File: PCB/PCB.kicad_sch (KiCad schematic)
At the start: 0 parts

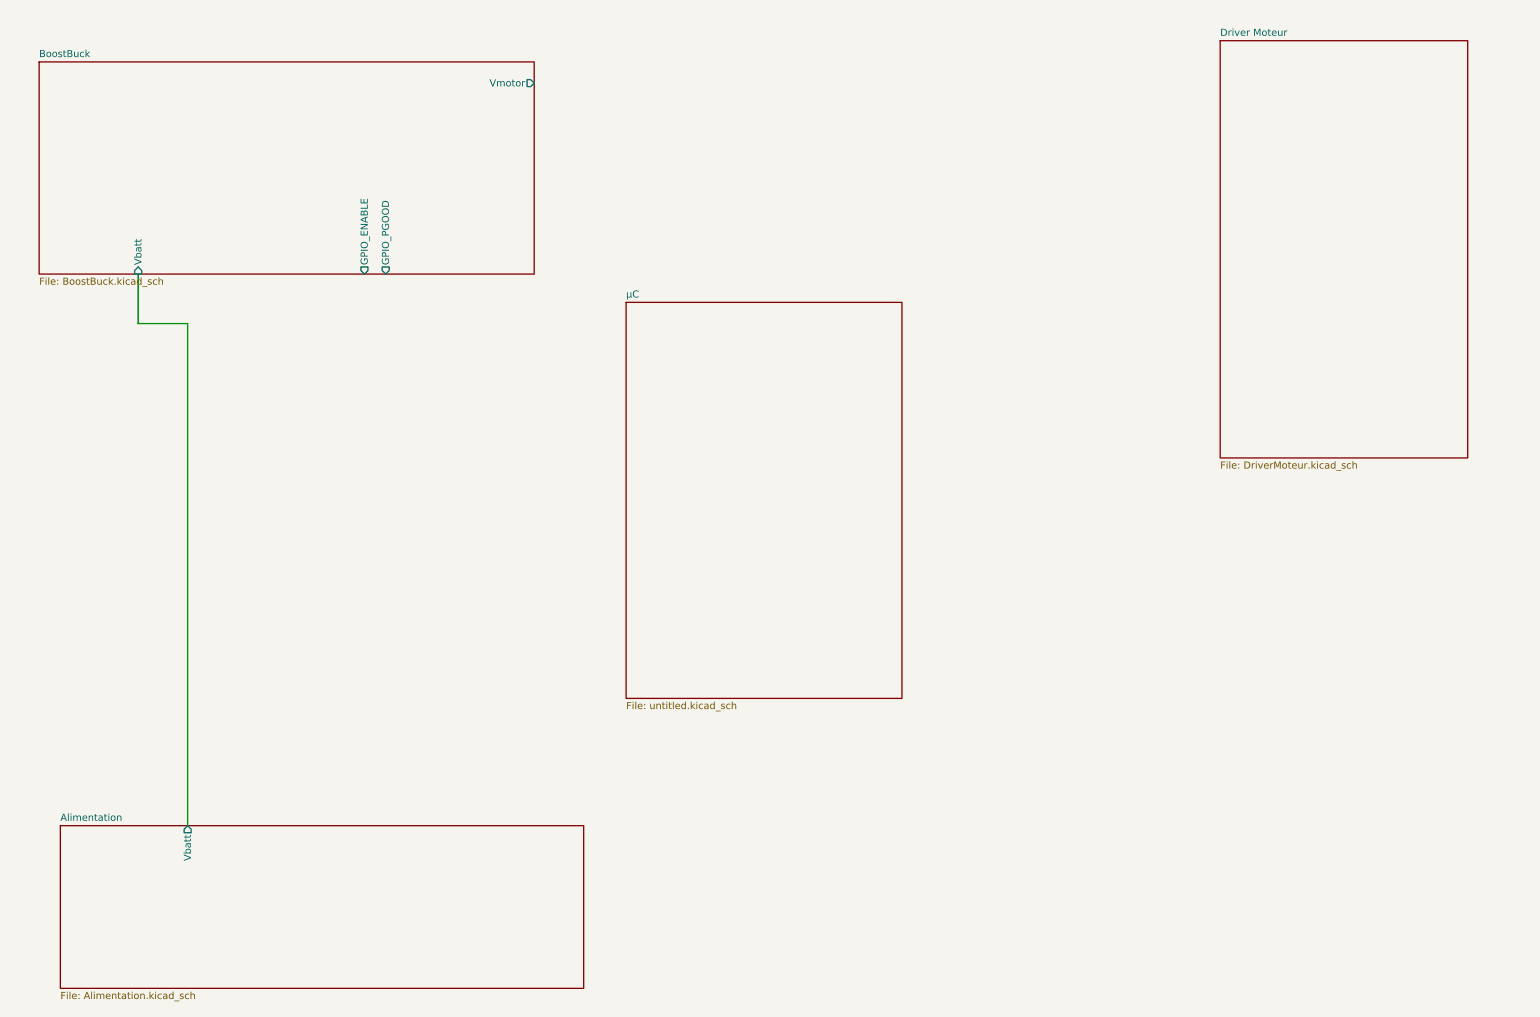
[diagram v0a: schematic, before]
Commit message: List of Modifs:
Corrected power supply sheet
Updated motor driver sheet
Added a project name to a lot of sheets (don't know why...)
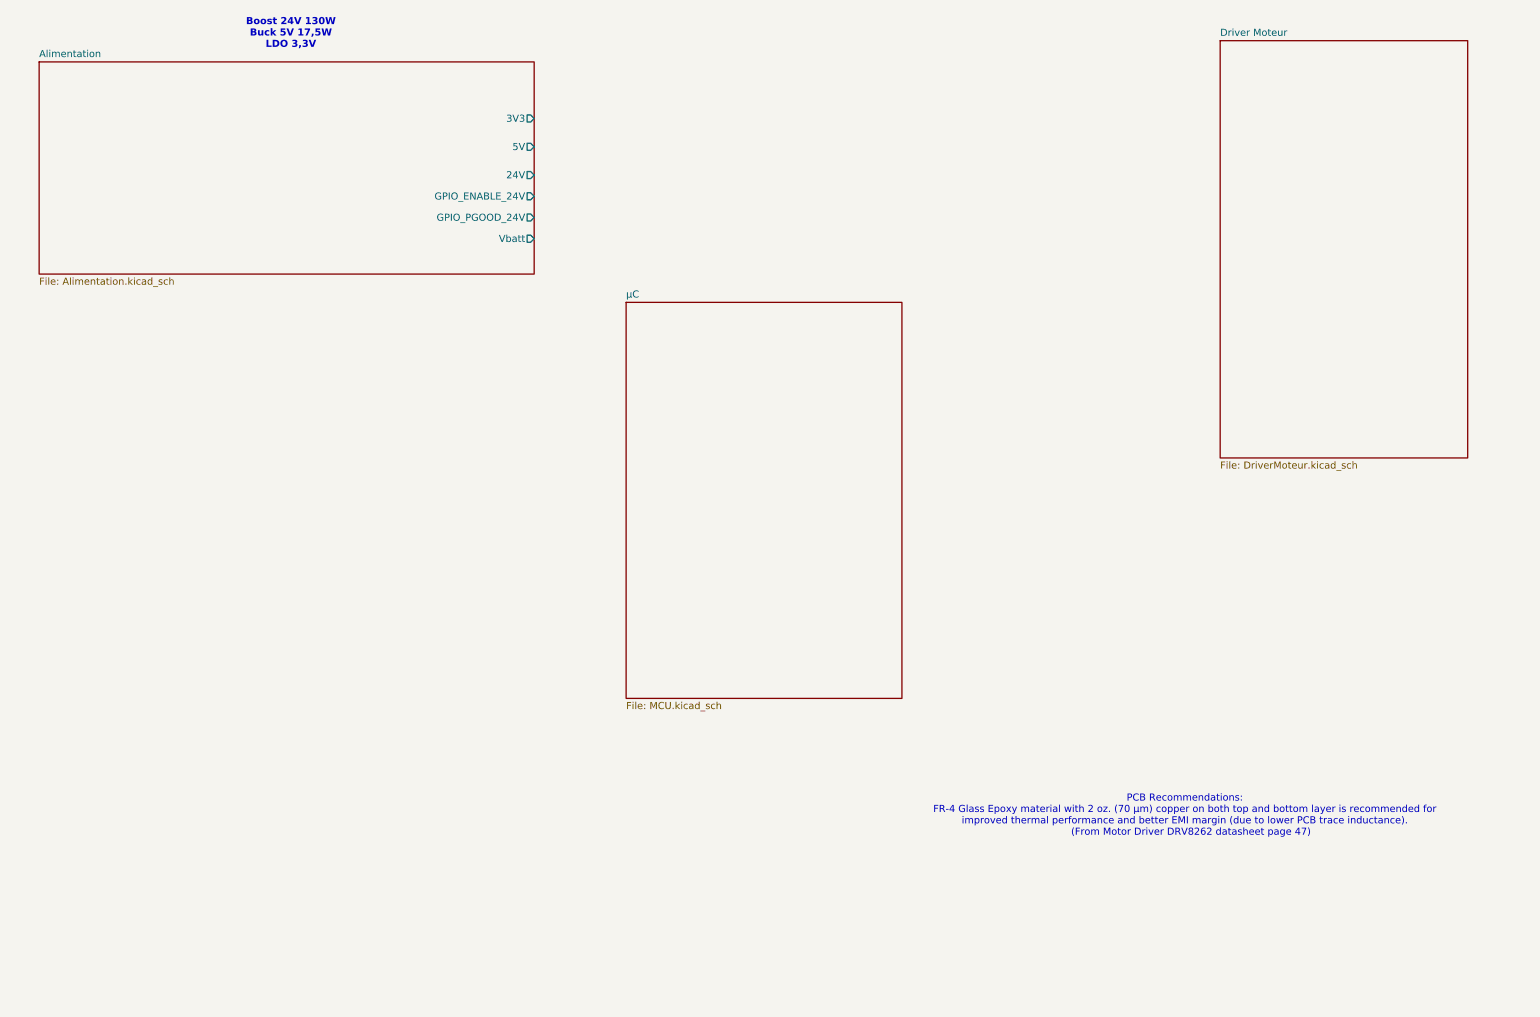
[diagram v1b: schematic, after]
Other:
- removed sheet BoostBuck
- sheet Alimentation ports: added 24V, 3V3, 5V, GPIO_ENABLE_24V, GPIO_PGOOD_24V; removed none
- sheet µC: file untitled.kicad_sch -> MCU.kicad_sch
- note added: "Boost 24V 130W Buck 5V 17,5W LDO 3,3V"
- note added: "PCB Recommendations: FR-4 Glass Epoxy material with 2 oz. (70 μm) copper on both top and bottom layer is recommended for improved thermal performance and better EMI margin (due to lower PCB trace inductance). (From Motor Driver DRV8262 datasheet page 47)"
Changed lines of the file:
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@@
 	(generator_version "9.0")
 	(paper "A4")
-	(wire
-		(pts
-			(xy 46.99 160.02) (xy 46.99 69.85)
-		)
-		(stroke
-			(width 0)
-			(type default)
+	(text "PCB Recommendations:\nFR-4 Glass Epoxy material with 2 oz. (70 μm) copper on both top and bottom layer is recommended for\nimproved thermal performance and better EMI margin (due to lower PCB trace inductance).\n	(From Motor Driver DRV8262 datasheet page 47)"
+		(exclude_from_sim no)
+		(at 226.06 158.242 0)
+		(effects
+			(font
+				(size 1.27 1.27)
+			)
 		)
 	)
-	(wire
-		(pts
-			(xy 46.99 69.85) (xy 38.1 69.85)
-		)
-		(stroke
-			(width 0)
-			(type default)
-		)
-	)
-	(wire
-		(pts
-			(xy 38.1 69.85) (xy 38.1 60.96)
-		)
-		(stroke
-			(width 0)
-			(type default)
+	(text "Boost 24V 130W\nBuck 5V 17,5W\nLDO 3,3V"
+		(exclude_from_sim no)
+		(at 65.532 17.78 0)
+		(effects
+			(font
+				(size 1.27 1.27)
+				(thickness 0.254)
+				(bold yes)
+			)
 		)
 	)
@@
 	)
 	(sheet
-		(at 24.13 160.02)
-		(size 93.98 29.21)
-		(exclude_from_sim no)
-		(in_bom yes)
-		(on_board yes)
-		(dnp no)
-		(fields_autoplaced yes)
-		(stroke
-			(width 0.1524)
-			(type solid)
-		)
-		(fill
-			(color 0 0 0 0.0000)
-		)
-		(property "Sheetname" "Alimentation"
-			(at 24.13 159.3084 0)
-			(effects
-				(font
-					(size 1.27 1.27)
-				)
-				(justify left bottom)
-			)
-		)
-		(property "Sheetfile" "Alimentation.kicad_sch"
-			(at 24.13 189.8146 0)
-			(effects
-				(font
-					(size 1.27 1.27)
-				)
-				(justify left top)
-			)
-		)
-		(pin "Vbatt" output
-			(at 46.99 160.02 90)
-			(effects
-				(font
-					(size 1.27 1.27)
-				)
-				(justify right)
-			)
-		)
-		(instances
-			(project "PCB"
-				(path "/117fd49e-499d-4b54-b58c-f6b538ecca4a"
-					(page "4")
-				)
-			)
-		)
-	)
-	(sheet
 		(at 125.73 66.04)
 		(size 49.53 71.12)
@@
 			)
 		)
-		(property "Sheetfile" "untitled.kicad_sch"
+		(property "Sheetfile" "MCU.kicad_sch"
 			(at 125.73 137.7446 0)
 			(effects
@@
 			(color 0 0 0 0.0000)
 		)
-		(property "Sheetname" "BoostBuck"
+		(property "Sheetname" "Alimentation"
 			(at 20.32 22.1484 0)
 			(effects
@@
 			)
 		)
-		(property "Sheetfile" "BoostBuck.kicad_sch"
+		(property "Sheetfile" "Alimentation.kicad_sch"
 			(at 20.32 61.5446 0)
 			(effects
@@
 			)
 		)
-		(pin "GPIO_ENABLE" output
-			(at 78.74 60.96 270)
+		(pin "3V3" output
+			(at 109.22 33.02 0)
 			(effects
 				(font
 					(size 1.27 1.27)
 				)
-				(justify left)
+				(justify right)
 			)
 		)
-		(pin "GPIO_PGOOD" output
-			(at 82.55 60.96 270)
+		(pin "5V" output
+			(at 109.22 38.1 0)
 			(effects
 				(font
 					(size 1.27 1.27)
 				)
-				(justify left)
+				(justify right)
 			)
 		)
-		(pin "Vbatt" input
-			(at 38.1 60.96 270)
+		(pin "24V" output
+			(at 109.22 43.18 0)
 			(effects
 				(font
 					(size 1.27 1.27)
 				)
-				(justify left)
+				(justify right)
 			)
 		)
-		(pin "Vmotor" output
-			(at 109.22 26.67 0)
+		(pin "GPIO_ENABLE_24V" output
+			(at 109.22 46.99 0)
 			(effects
 				(font
+					(size 1.27 1.27)
+				)
+				(justify right)
+			)
+		)
+		(pin "GPIO_PGOOD_24V" output
+			(at 109.22 50.8 0)
+			(effects
+				(font
+					(size 1.27 1.27)
+				)
+				(justify right)
+			)
+		)
+		(pin "Vbatt" output
+			(at 109.22 54.61 0)
+			(effects
+				(font

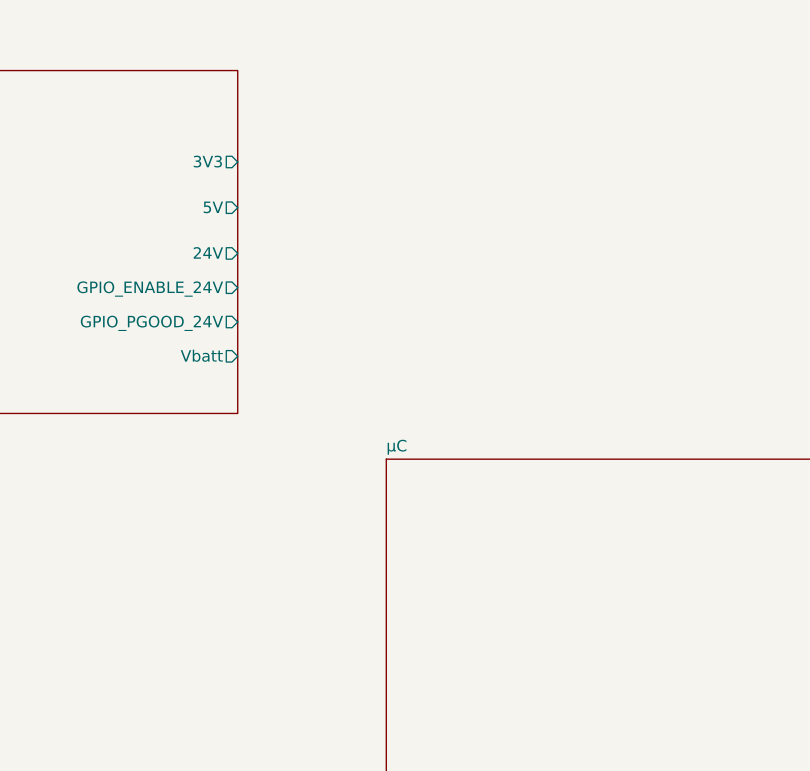
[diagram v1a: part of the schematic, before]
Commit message: Updated MCU sheet
Added decoupling capacitors
Linked Ethernet to MCU
Started Usb linking to MCU
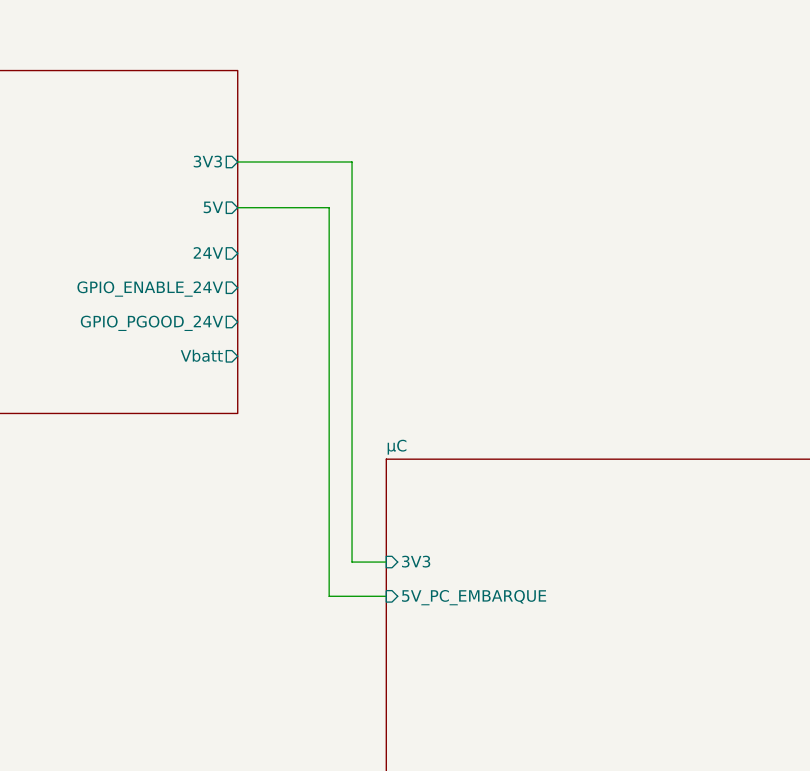
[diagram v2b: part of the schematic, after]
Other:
- sheet µC ports: added 3V3, 5V_PC_EMBARQUE; removed none
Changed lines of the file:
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@@
+		)
+	)
+	(wire
+		(pts
+			(xy 121.92 77.47) (xy 125.73 77.47)
+		)
+		(stroke
+			(width 0)
+			(type default)
+		)
+	)
+	(wire
+		(pts
+			(xy 109.22 33.02) (xy 121.92 33.02)
+		)
+		(stroke
+			(width 0)
+			(type default)
+		)
+	)
+	(wire
+		(pts
+			(xy 119.38 81.28) (xy 125.73 81.28)
+		)
+		(stroke
+			(width 0)
+			(type default)
+		)
+	)
+	(wire
+		(pts
+			(xy 119.38 38.1) (xy 119.38 81.28)
+		)
+		(stroke
+			(width 0)
+			(type default)
+		)
+	)
+	(wire
+		(pts
+			(xy 121.92 33.02) (xy 121.92 77.47)
+		)
+		(stroke
+			(width 0)
+			(type default)
+		)
+	)
+	(wire
+		(pts
+			(xy 109.22 38.1) (xy 119.38 38.1)
+		)
+		(stroke
+			(width 0)
+			(type default)
 		)
 	)
@@
 			)
 		)
+		(pin "3V3" input
+			(at 125.73 77.47 180)
+			(effects
+				(font
+					(size 1.27 1.27)
+				)
+				(justify left)
+			)
+		)
+		(pin "5V_PC_EMBARQUE" input
+			(at 125.73 81.28 180)
+			(effects
+				(font
+					(size 1.27 1.27)
+				)
+				(justify left)
+			)
+		)

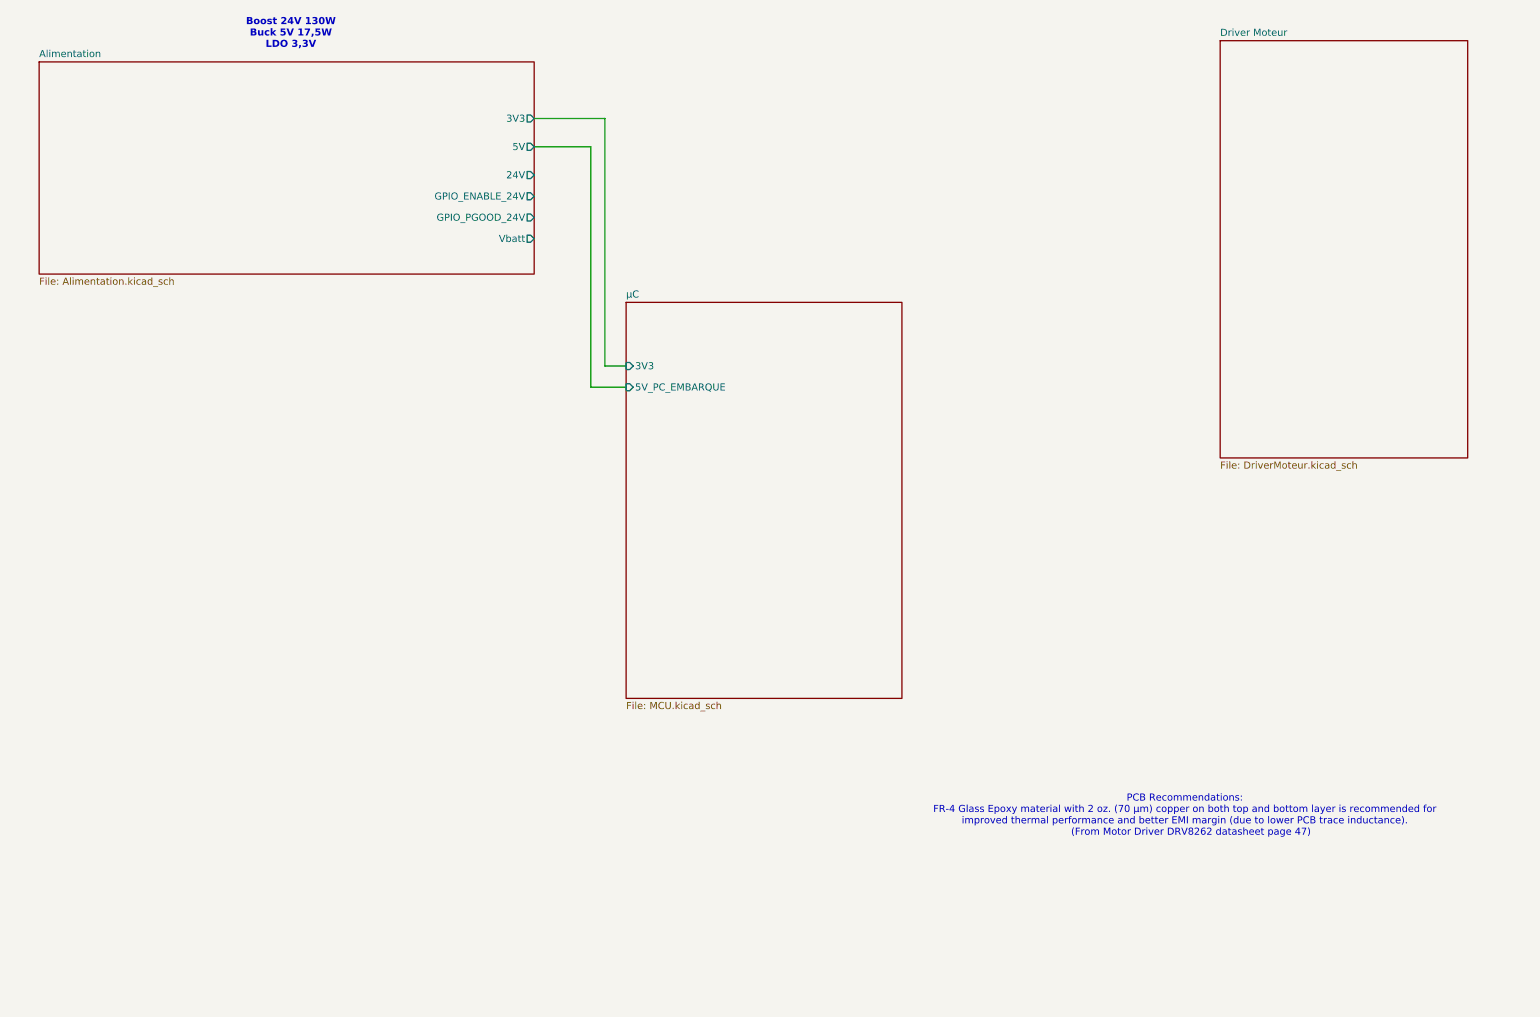
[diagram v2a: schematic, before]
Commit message: Updated a lot of stuff:
Added encoders,
Added 5V power supply for actuators
Added 12V power supply for actuators
Renamed sheets to be clearer
Added usb debug
Modify MCU sheet to be A3 format
Linked some pins
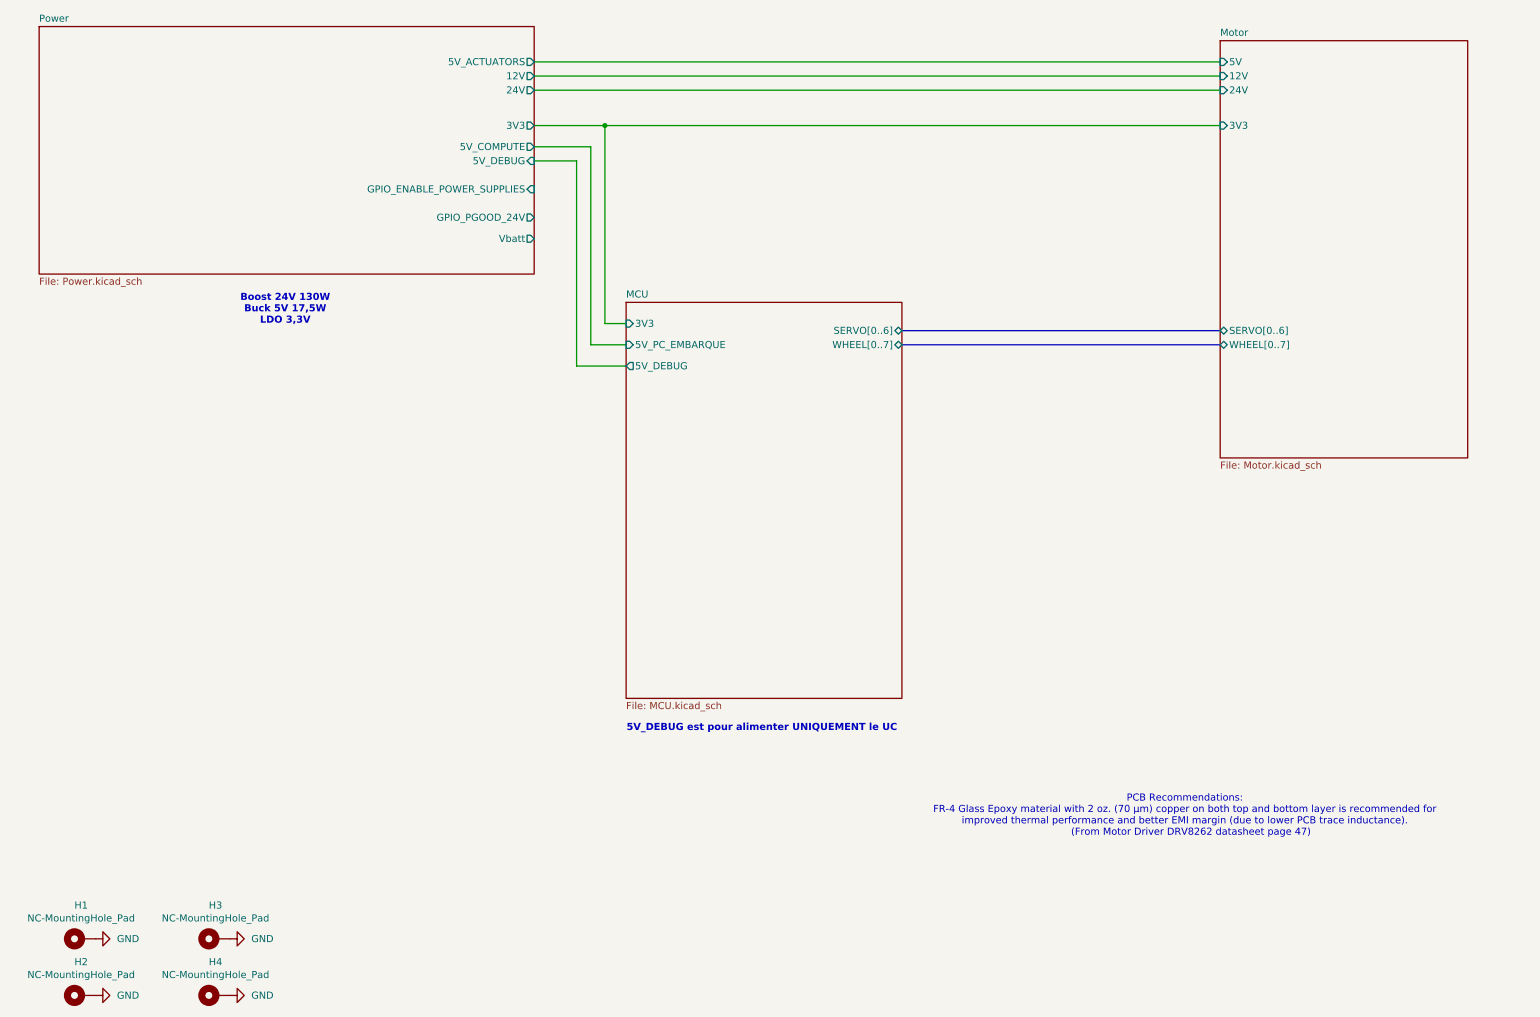
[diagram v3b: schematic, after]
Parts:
- added H1, H2, H3, H4: NC-MountingHole_Pad, MountingHole:MountingHole_4.3mm_M4_DIN965_Pad_TopBottom, symbol Mechanical:MountingHole_Pad
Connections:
- new net GND: H1.1, H2.1, H3.1, H4.1
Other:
- sheet Alimentation renamed Power
- sheet Driver Moteur renamed Motor
- sheet µC renamed MCU
- sheet MCU ports: added 5V_DEBUG, SERVO[0..6], WHEEL[0..7]; removed none
- sheet Motor: file DriverMoteur.kicad_sch -> Motor.kicad_sch
- sheet Motor ports: added 12V, 24V, 3V3, 5V, SERVO[0..6], WHEEL[0..7]; removed none
- sheet Power: file Alimentation.kicad_sch -> Power.kicad_sch
- sheet Power ports: added 12V, 5V_ACTUATORS, 5V_COMPUTE, 5V_DEBUG, GPIO_ENABLE_POWER_SUPPLIES; removed 5V, GPIO_ENABLE_24V
- note added: "5V_DEBUG est pour alimenter UNIQUEMENT le UC"
